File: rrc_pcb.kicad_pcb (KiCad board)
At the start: 2 copper layers, 139 x 49 mm, 13 parts, among them J1 Voltage Regulator Input, J2 Conn_01x03_Male, U1 ADXL357Z, U2 Teensy3.6-teensy, U3 BN220-GPS, U4 MS5611, U5 logo

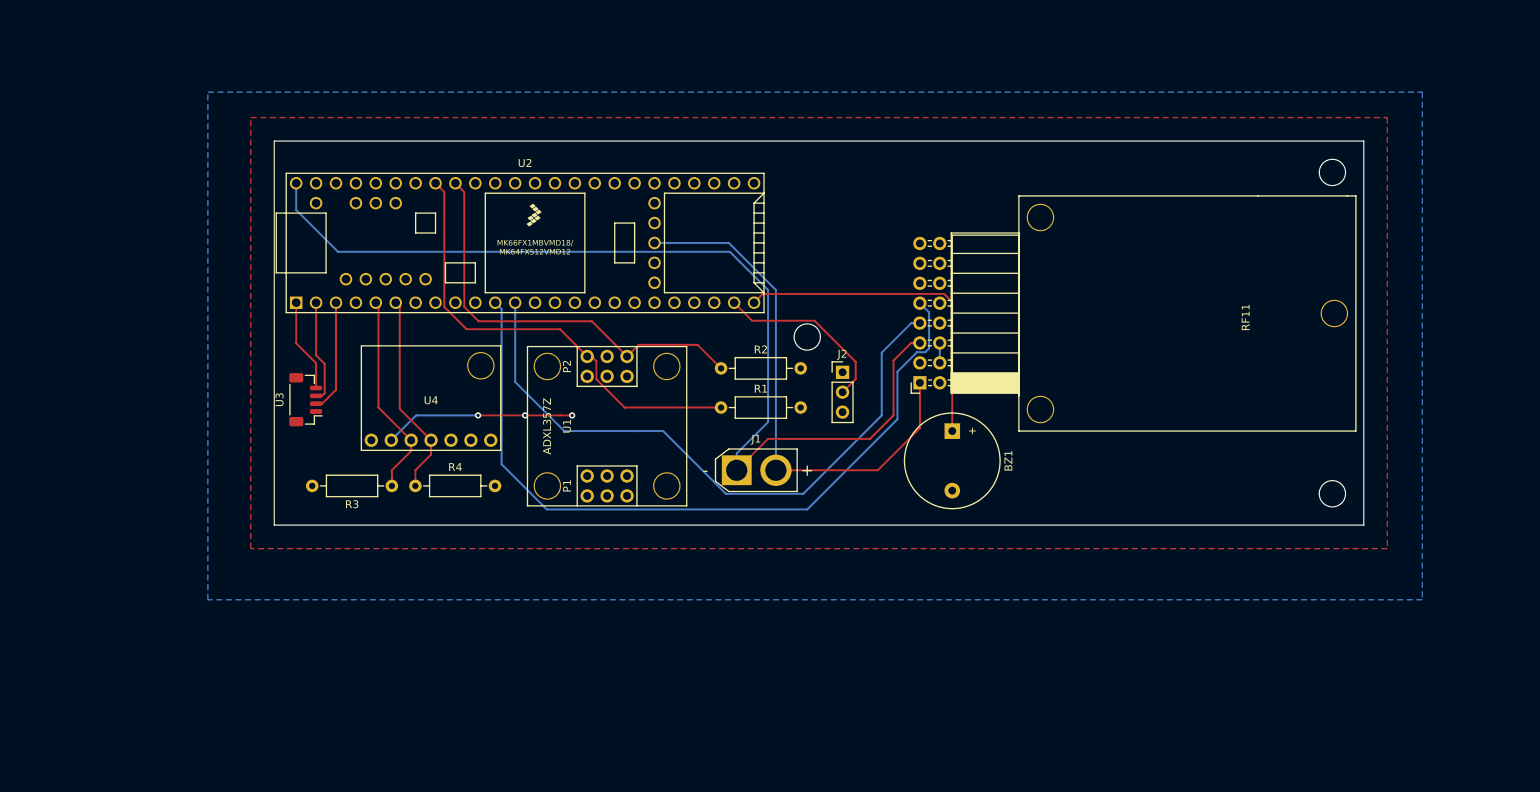
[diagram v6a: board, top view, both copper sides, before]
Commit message: moved standoffs around for better placement structurally , PCB is ready to go
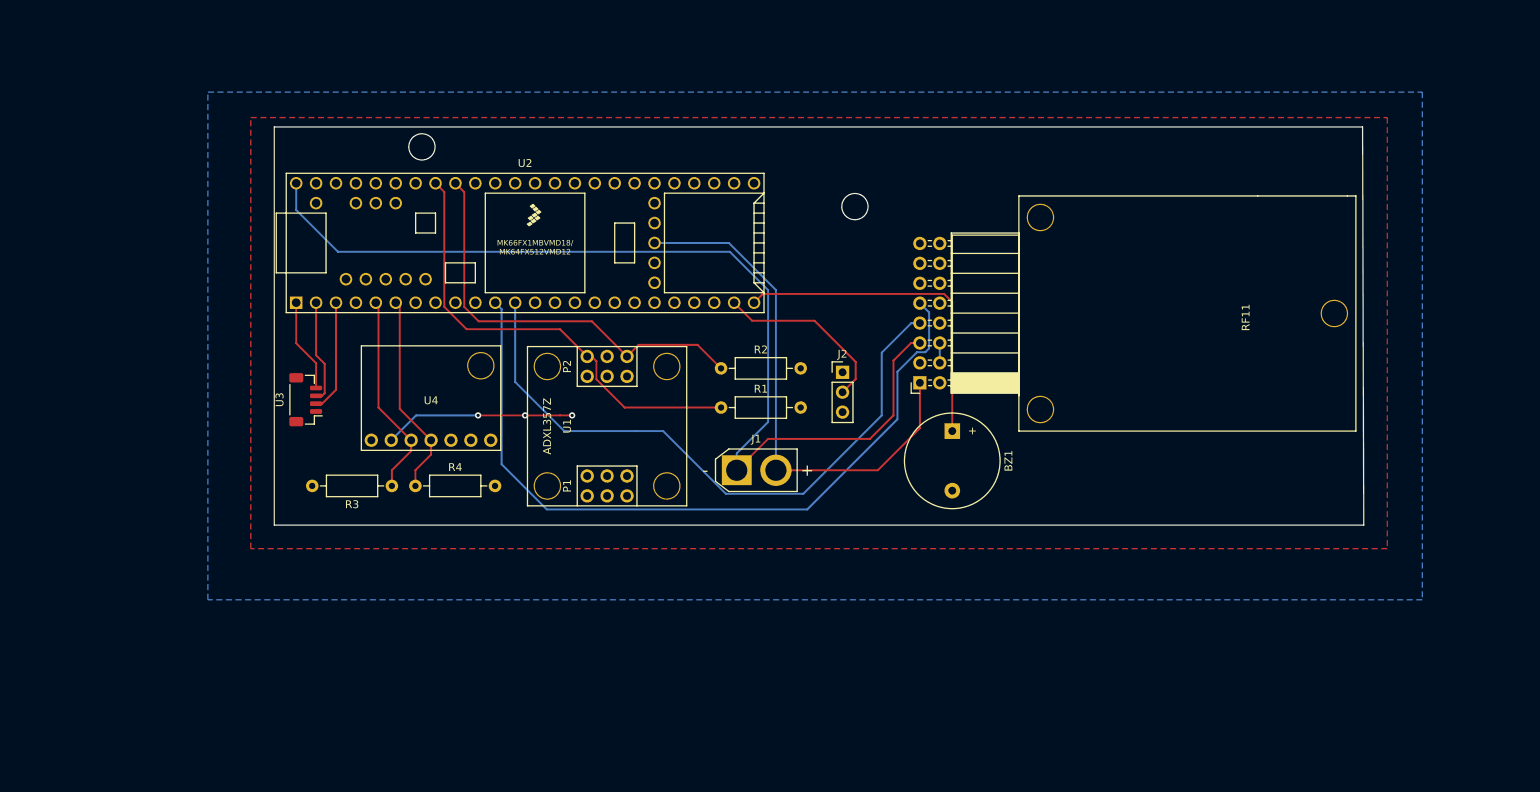
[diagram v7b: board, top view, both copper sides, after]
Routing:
- net (no net): vias 3 -> 2
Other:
- board size 139 x 49 mm -> 139 x 50.8 mm
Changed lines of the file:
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@@
-(kicad_pcb (version 20171130) (host pcbnew "(5.1.8)-1")
+(kicad_pcb (version 20171130) (host pcbnew "(5.1.10)-1")
   (general
     (thickness 1.6)
     (drawings 4)
-    (tracks 104)
+    (tracks 103)
     (zones 0)
     (modules 13)
@@
       (effects (font (size 1 1) (thickness 0.15)))
     )
-    (fp_text user %R (at 0 2.54 90) (layer F.Fab)
-      (effects (font (size 1 1) (thickness 0.15)))
-    )
     (fp_line (start -0.635 -1.27) (end 1.27 -1.27) (layer F.Fab) (width 0.1))
     (fp_line (start 1.27 -1.27) (end 1.27 6.35) (layer F.Fab) (width 0.1))
@@
     (fp_line (start 1.8 6.85) (end 1.8 -1.8) (layer F.CrtYd) (width 0.05))
     (fp_line (start 1.8 -1.8) (end -1.8 -1.8) (layer F.CrtYd) (width 0.05))
+    (fp_text user %R (at 0 2.54 90) (layer F.Fab)
+      (effects (font (size 1 1) (thickness 0.15)))
+    )
     (pad 3 thru_hole oval (at 0 5.08) (size 1.7 1.7) (drill 1) (layers *.Cu *.Mask)
       (net 3 T_VCC))
@@
     )
   )
-  (gr_line (start 58 127) (end 58 78) (layer Edge.Cuts) (width 0.05))
+  (gr_line (start 58 127) (end 58 76.2) (layer Edge.Cuts) (width 0.05))
   (gr_line (start 197 127) (end 58 127) (layer Edge.Cuts) (width 0.05))
-  (gr_line (start 197 78) (end 197 127) (layer Edge.Cuts) (width 0.05))
-  (gr_line (start 58 78) (end 197 78) (layer Edge.Cuts) (width 0.05))
-  (via (at 126 103) (size 3.5) (drill 3.2) (layers F.Cu B.Cu) (net 0))
-  (via (at 193 123) (size 3.5) (drill 3.2) (layers F.Cu B.Cu) (net 0))
-  (via (at 193 82) (size 3.5) (drill 3.2) (layers F.Cu B.Cu) (net 0))
+  (gr_line (start 196.85 76.2) (end 197 127) (layer Edge.Cuts) (width 0.05))
+  (gr_line (start 58 76.2) (end 196.85 76.2) (layer Edge.Cuts) (width 0.05))
+  (via (at 132.08 86.36) (size 3.5) (drill 3.2) (layers F.Cu B.Cu) (net 0))
+  (via (at 76.835 78.74) (size 3.5) (drill 3.2) (layers F.Cu B.Cu) (net 0))
   (segment (start 122 120) (end 135 120) (width 0.25) (layer F.Cu) (net 1))
   (segment (start 135 120) (end 140.36812 114.63188) (width 0.25) (layer F.Cu) (net 1))
@@
   (segment (start 140.742123 108.127259) (end 139.872741 108.127259) (width 0.25) (layer B.Cu) (net 1))
   (segment (start 140.36812 114.63188) (end 140.36812 108.84226) (width 0.25) (layer F.Cu) (net 1))
-  (segment (start 60.79 86.79) (end 60.79 83.38) (width 0.25) (layer B.Cu) (net 2))
-  (segment (start 66.125001 92.125001) (end 60.79 86.79) (width 0.25) (layer B.Cu) (net 2))
   (segment (start 116.125001 92.125001) (end 66.125001 92.125001) (width 0.25) (layer B.Cu) (net 2))
   (segment (start 121 97) (end 116.125001 92.125001) (width 0.25) (layer B.Cu) (net 2))
@@
   (segment (start 121 116) (end 134 116) (width 0.25) (layer F.Cu) (net 2))
   (segment (start 117 120) (end 121 116) (width 0.25) (layer F.Cu) (net 2))
+  (segment (start 60.79 86.79) (end 60.79 83.38) (width 0.25) (layer B.Cu) (net 2))
+  (segment (start 66.125001 92.125001) (end 60.79 86.79) (width 0.25) (layer B.Cu) (net 2))
   (segment (start 99.095001 108.396003) (end 99.095001 106.095001) (width 0.25) (layer F.Cu) (net 4))
   (segment (start 102.698998 112) (end 99.095001 108.396003) (width 0.25) (layer F.Cu) (net 4))
@@
   (segment (start 87 99.43) (end 87 119.231002) (width 0.25) (layer B.Cu) (net 14))
   (segment (start 86.19 98.62) (end 87 99.43) (width 0.25) (layer B.Cu) (net 14))
-  (segment (start 63.325 109.5) (end 63.325 106.325) (width 0.25) (layer F.Cu) (net 22))
-  (segment (start 60.79 103.79) (end 60.79 98.62) (width 0.25) (layer F.Cu) (net 22))
-  (segment (start 63.325 106.325) (end 60.79 103.79) (width 0.25) (layer F.Cu) (net 22))
   (segment (start 76.09 113) (end 84 113) (width 0.25) (layer B.Cu) (net 22))
   (via (at 84 113) (size 0.8) (drill 0.4) (layers F.Cu B.Cu) (net 22))
@@
   (segment (start 94.469002 113) (end 96 113) (width 0.25) (layer F.Cu) (net 22))
   (segment (start 90 113) (end 94.469002 113) (width 0.25) (layer F.Cu) (net 22))
+  (segment (start 63.325 109.5) (end 63.325 106.325) (width 0.25) (layer F.Cu) (net 22))
+  (segment (start 63.325 106.325) (end 60.79 103.79) (width 0.25) (layer F.Cu) (net 22))
+  (segment (start 60.79 103.79) (end 60.79 98.62) (width 0.25) (layer F.Cu) (net 22))
   (segment (start 64.42501 110.17499) (end 64.42501 106.42501) (width 0.25) (layer F.Cu) (net 44))
   (segment (start 64.1 110.5) (end 64.42501 110.17499) (width 0.25) (layer F.Cu) (net 44))

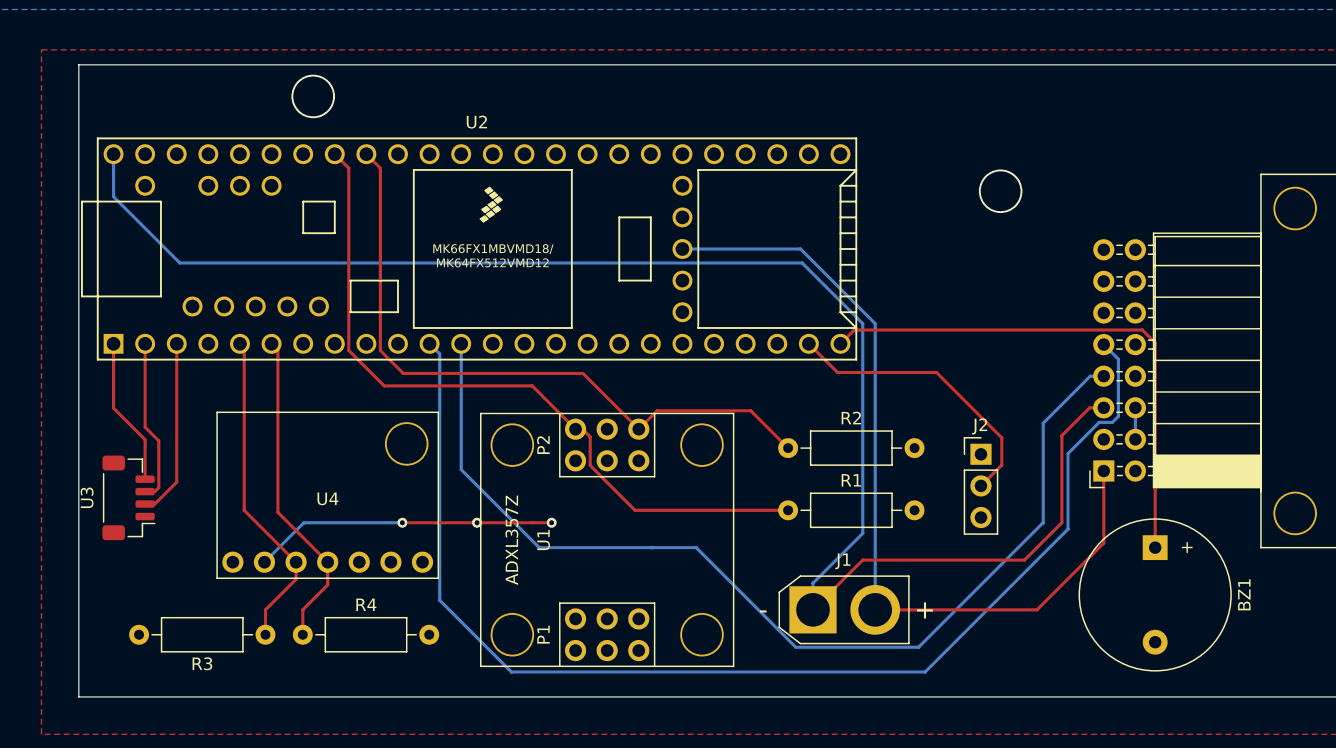
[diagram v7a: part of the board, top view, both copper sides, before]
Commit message: fixed prototype mistakes
changed some drill holes positions
changed GPS connector
changed teensy used pins
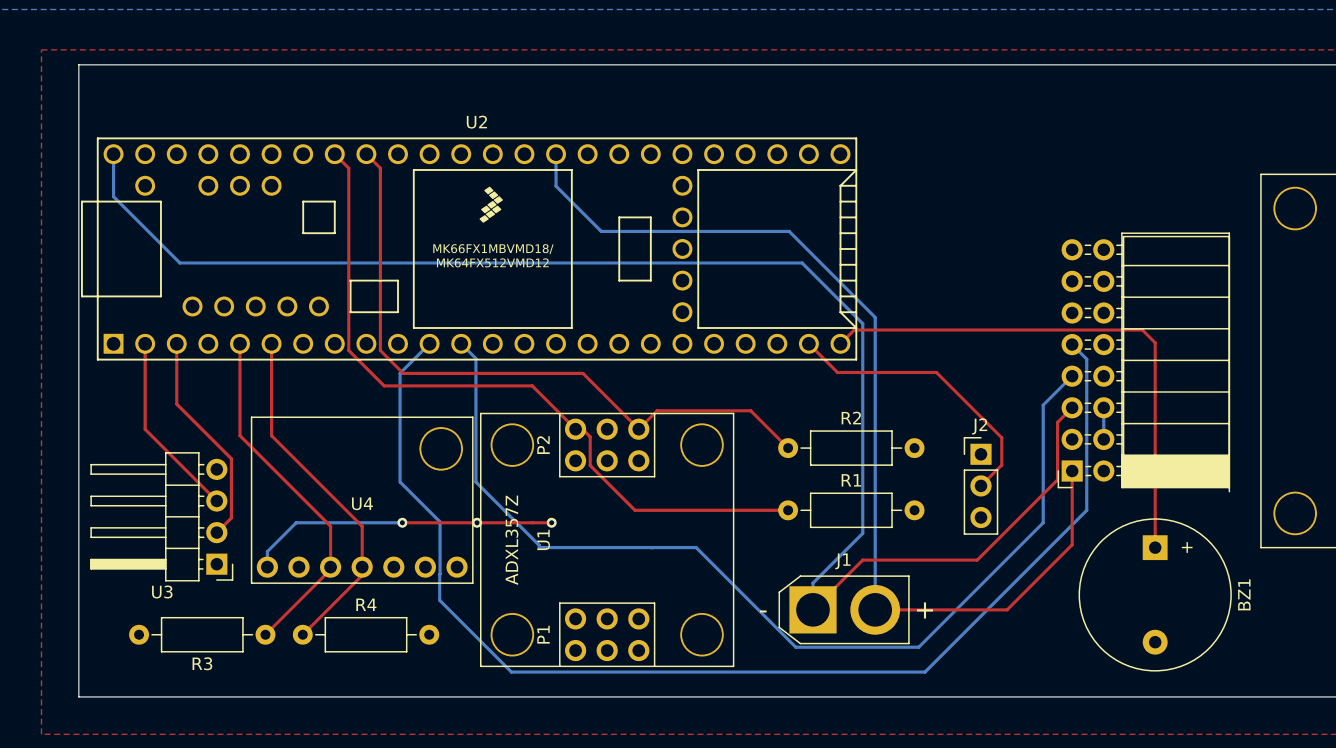
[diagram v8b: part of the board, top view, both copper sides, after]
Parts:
- U3: footprint Connector_JST:JST_SH_BM04B-SRSS-TB_1x04-1MP_P1.00mm_Vertical -> Connector_PinHeader_2.54mm:PinHeader_1x04_P2.54mm_Horizontal
- moved U3 8.87 mm to (69.1, 116.3), turned to 180 degrees
- moved U4 2.80 mm to (80.8, 120.4)
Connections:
- U2 pad 15: Net-(U2-Pad15) -> T_VCC
- U2 pad 26: T_VCC -> Net-(U2-Pad26)
- U2 pad 27: GND -> Net-(U2-Pad27)
- U2 pad 39: Net-(U2-Pad39) -> GND
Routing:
- net T_GND: track 36.3 -> 0.00 mm, vias 3 -> 0
- net T_VCC: track 0.00 -> 25.1 mm, vias 0 -> 3
- net GND: track 68.2 -> 80.0 mm
- net VCC: track 126.7 -> 122.8 mm
- net Net-(U2-Pad3): track 14.4 -> 17.5 mm
- net Net-(R4-Pad1): track 26.1 -> 29.1 mm
- net Net-(R3-Pad1): track 26.3 -> 29.0 mm
- net Net-(U2-Pad2): track 13.2 -> 15.0 mm
- net Net-(RF11-Pad7): track 81.5 -> 79.8 mm
- net (no net): vias 2 -> 0
